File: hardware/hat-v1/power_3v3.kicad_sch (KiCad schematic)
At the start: 29 parts, among them Q4 CSD17578Q3A, Q5 CSD17578Q3A, Q8 BSS138, Q9 BSS138, U5 LM74700QDBVRQ1, U6 LM74700QDBVRQ1, U7 TPS62933FDRLR, U8 INA226AIDGSR

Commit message: HAT v1 schematic: apply adversarial review (power + digital/security/DFM)
AUTO-ON above buck EN window, BENCH no longer blocks power-off, OVP moved
to 19.2 V with input damper, Tier A parts DNP for JLC, debug links
removable for production, antenna short limited, stock footprints where
available, cap ratings/DC-bias fixes, CONSOLE_TX/RX naming.

Co-Authored-By: Claude Opus 5.5 <noreply@anthropic.com>
Claude-Session: https://claude.ai/code/session_01MLRuxTEmuMV82xcNLE62jW
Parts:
- added C32: 2.2n 16V, Capacitor_SMD:C_0402_1005Metric, symbol batman:C
- C20, C21: value 100n 16V -> 220n 25V X7R; footprint Capacitor_SMD:C_0402_1005Metric -> Capacitor_SMD:C_0603_1608Metric
- C22, C23: value 10u 35V X5R -> 10u 50V X7R; footprint Capacitor_SMD:C_1206_3216Metric -> Capacitor_SMD:C_1210_3225Metric
- JP1, JP2: now left out of the parts list
- L2: footprint Inductor_SMD:L_Coilcraft_XGL4030 -> Inductor_SMD:L_Coilcraft_XxL4030
- Q4, Q5: footprint batman:TI_VSON-CLIP-8_3.3x3.3mm -> Package_SON:VSON-8_3.3x3.3mm_P0.65mm_NexFET
- R23: value 100k -> 4.7M; Note (none) -> high value: BENCH (Q9 on) must not load LTC_ENB, or Q7 cann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
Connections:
- net EN_3V3: now also C32.1
- net GND: now also C32.2
- net OR_NODE: no longer Q4.6 (D), Q4.7 (D), Q4.8 (D), Q4.9 (D), Q5.6 (D), Q5.7 (D), Q5.8 (D), Q5.9 (D)
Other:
- moved on the sheet: JP2

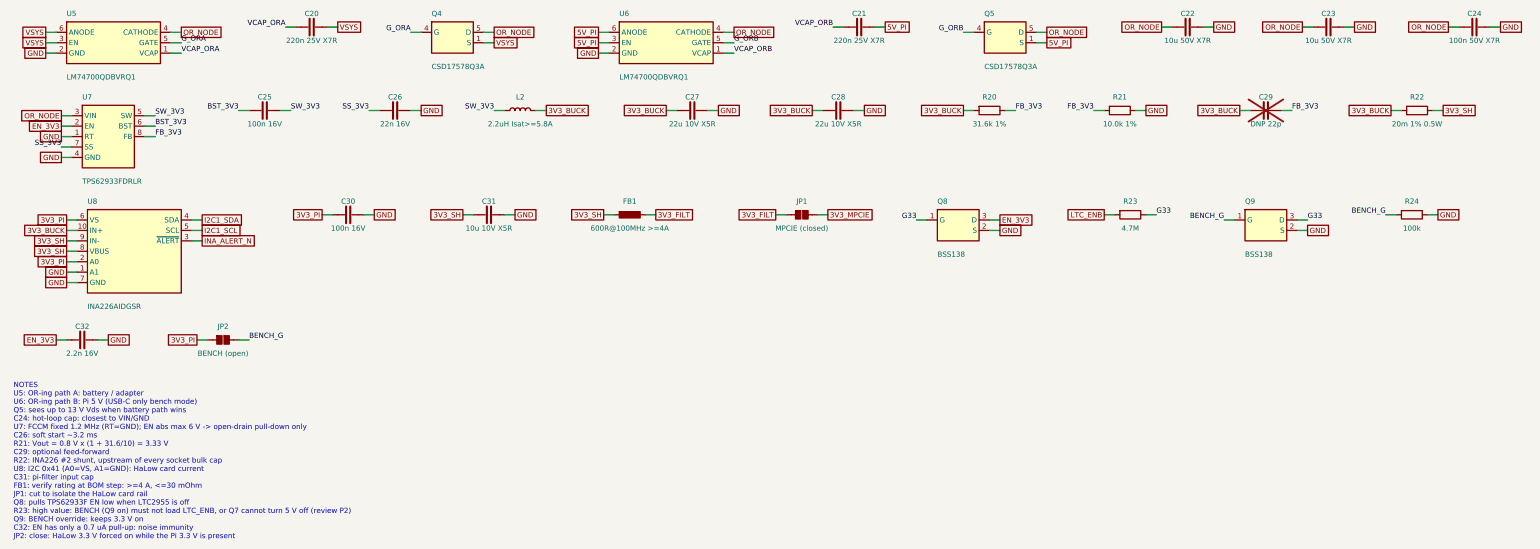
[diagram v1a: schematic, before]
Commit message: HAT v1: option D power tree - HaLow 3.3 V buck fed from the Pi 5 V rail
- TPS62933F input moved from the OR node to 5V_PI (HAT 5 V buck or Pi USB-C),
  as on the WM1302 HAT: the HaLow card still runs on USB-C only
- EN pulled up to the Pi 3.3 V through 100k: no back-feed into an unpowered Pi,
  HAT+ STANDBY turns the card off; LTC2955 off already removes 5 V
- removed: LM74700 x2 + FET x2 + VCAP x2 (OR-ing), BENCH jumper + Q9/R24, Q8,
  HAT ID EEPROM + WP jumper + pull-ups + decoupling, OR_NODE test point
- kept the battery-present divider (spec review #22)
- checker: HaLow EN set points; spec 5.5.5 power tree review; re-placed board

Co-Authored-By: Claude Opus 5.5 <noreply@anthropic.com>
Claude-Session: https://claude.ai/code/session_01MLRuxTEmuMV82xcNLE62jW
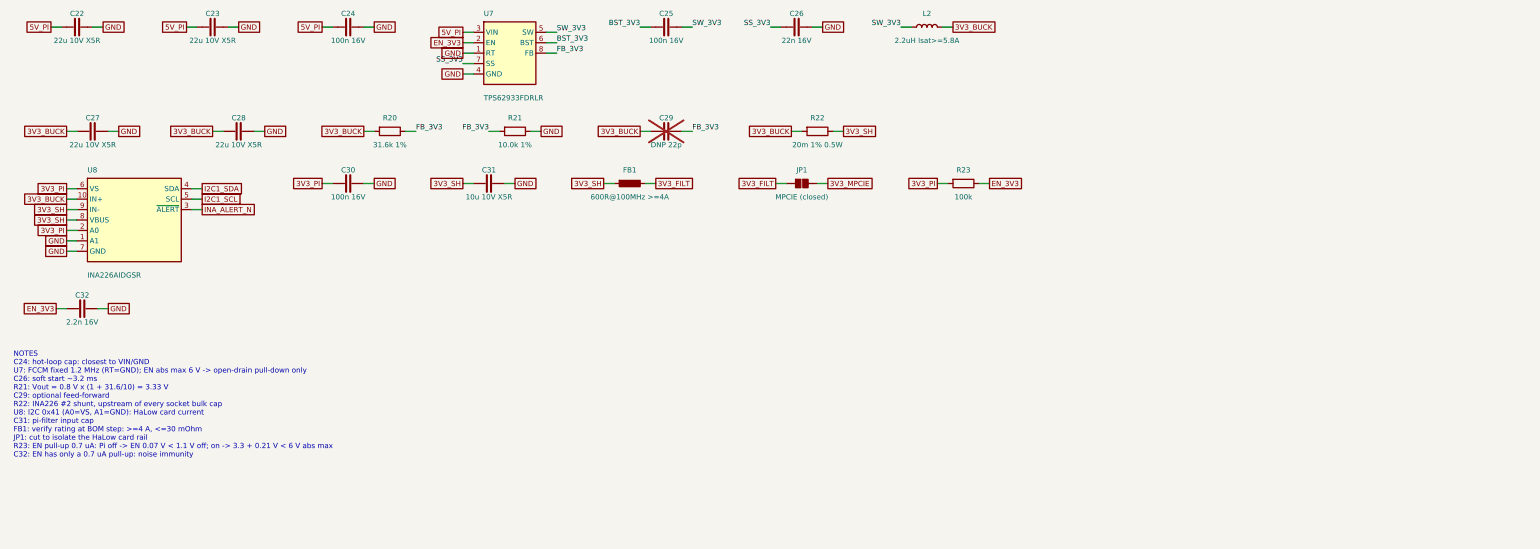
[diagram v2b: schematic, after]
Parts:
- removed C20, C21: 220n 25V X7R, Capacitor_SMD:C_0603_1608Metric, symbol batman:C
- removed JP2: BENCH (open), Jumper:SolderJumper-2_P1.3mm_Open_RoundedPad1.0x1.5mm, symbol batman:SJ
- removed Q4, Q5: CSD17578Q3A, Package_SON:VSON-8_3.3x3.3mm_P0.65mm_NexFET, symbol batman:NMOS_SON8
- removed Q8, Q9: BSS138, Package_TO_SOT_SMD:SOT-23, symbol batman:NMOS
- removed R24: 100k, Resistor_SMD:R_0402_1005Metric, symbol batman:R
- removed U5, U6: LM74700QDBVRQ1, Package_TO_SOT_SMD:SOT-23-6, symbol batman:LM74700
- C22, C23: value 10u 50V X7R -> 22u 10V X5R; footprint Capacitor_SMD:C_1210_3225Metric -> Capacitor_SMD:C_0805_2012Metric
- C24: value 100n 50V X7R -> 100n 16V
- R23: value 4.7M -> 100k; Note high value: BENCH (Q9 on) must not load LTC_ENB, or Q7 cann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 -> EN pull-up 0.7 uA: Pi off -> EN 0.07 V < 1.1 V off; on -> 3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
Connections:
- net G33 is gone; now on net EN_3V3: R23.2
- net LTC_ENB is gone; now on net 3V3_PI: R23.1
- net OR_NODE is gone; now on net 5V_PI: C22.1, C23.1, C24.1, U7.3 (VIN)
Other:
- note added: "NOTES C24: hot-loop cap: closest to VIN/GND U7: FCCM fixed 1.2 MHz (RT=GND); EN abs max 6 V -> open-drain pull-down only C26: soft start ~3.2 ms R21: Vout = 0.8 V x (1 + 31.6/10) = 3.33 V C29: optional feed-forward R22: INA226 #2 shunt, upstream of every socket bulk cap U8: I2C 0x41 (A0=VS, A1=GND): HaLow card current C31: pi-filter input cap FB1: verify rating at BOM step: >=4 A, <=30 mOhm JP1: 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"
- note removed: "NOTES U5: OR-ing path A: battery / adapter U6: OR-ing path B: Pi 5 V (USB-C only bench mode) Q5: sees up to 13 V Vds when battery path wins C24: hot-loop cap: closest to VIN/GND U7: FCCM fixed 1.2 MHz (RT=GND); EN abs max 6 V -> open-drain pull-down only C26: soft start ~3.2 ms R21: Vout = 0.8 V x (1 + 31.6/10) = 3.33 V C29: optional feed-forward R22: INA226 #2 shunt, upstream of every socket bul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"
- moved on the sheet: C22, C23, C24, C25, C26, C27, C28, C29, C30, C31, C32, FB1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
